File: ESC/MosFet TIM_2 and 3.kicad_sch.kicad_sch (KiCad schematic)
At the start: 34 parts, among them J3 Conn_01x03, Q1 BSC028N06LS3, Q2 BSC028N06LS3, U2 IRS2101

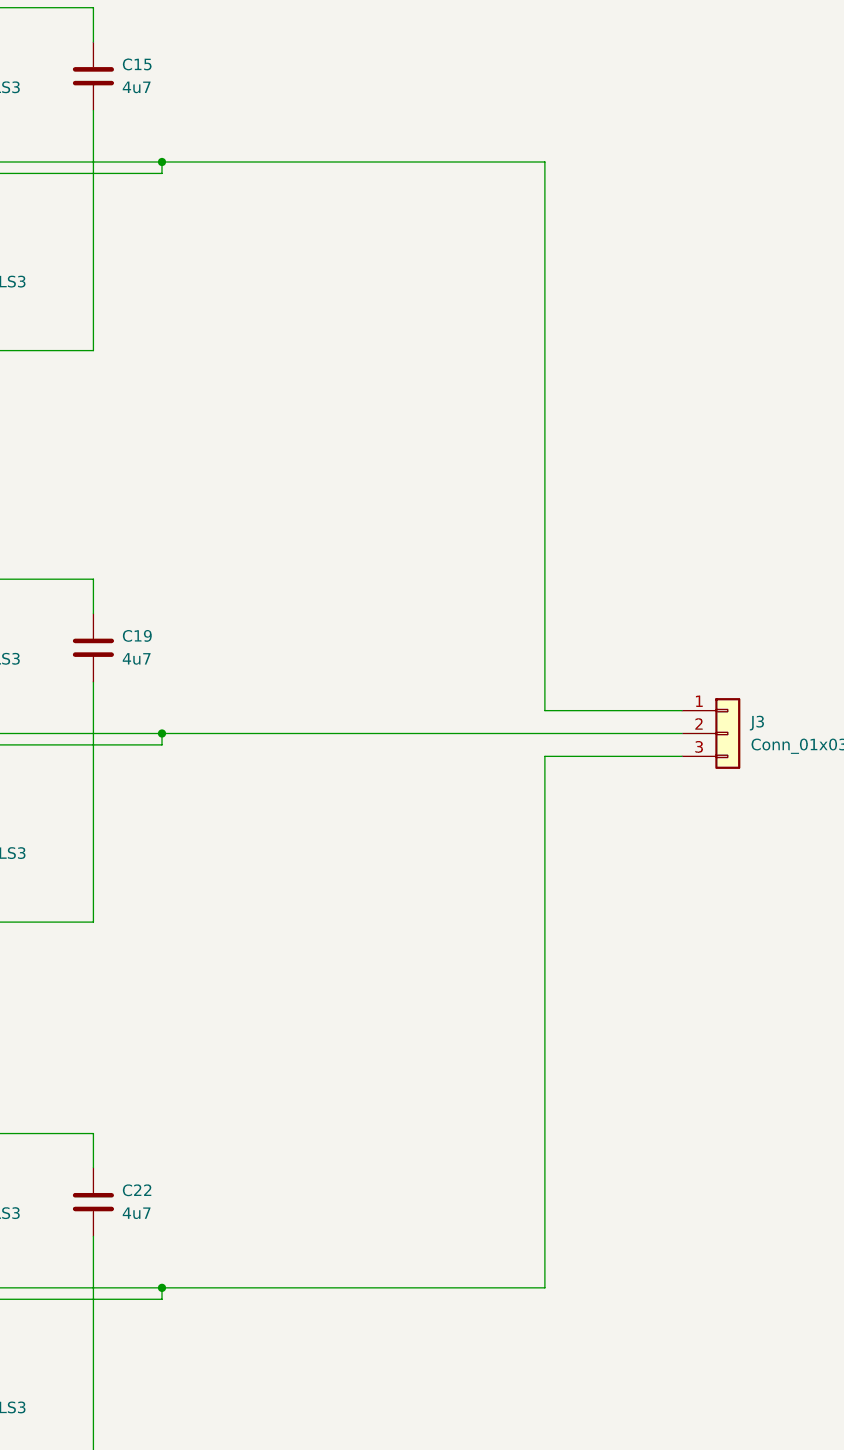
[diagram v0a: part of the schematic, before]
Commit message: finished a mockup of the pcb layout
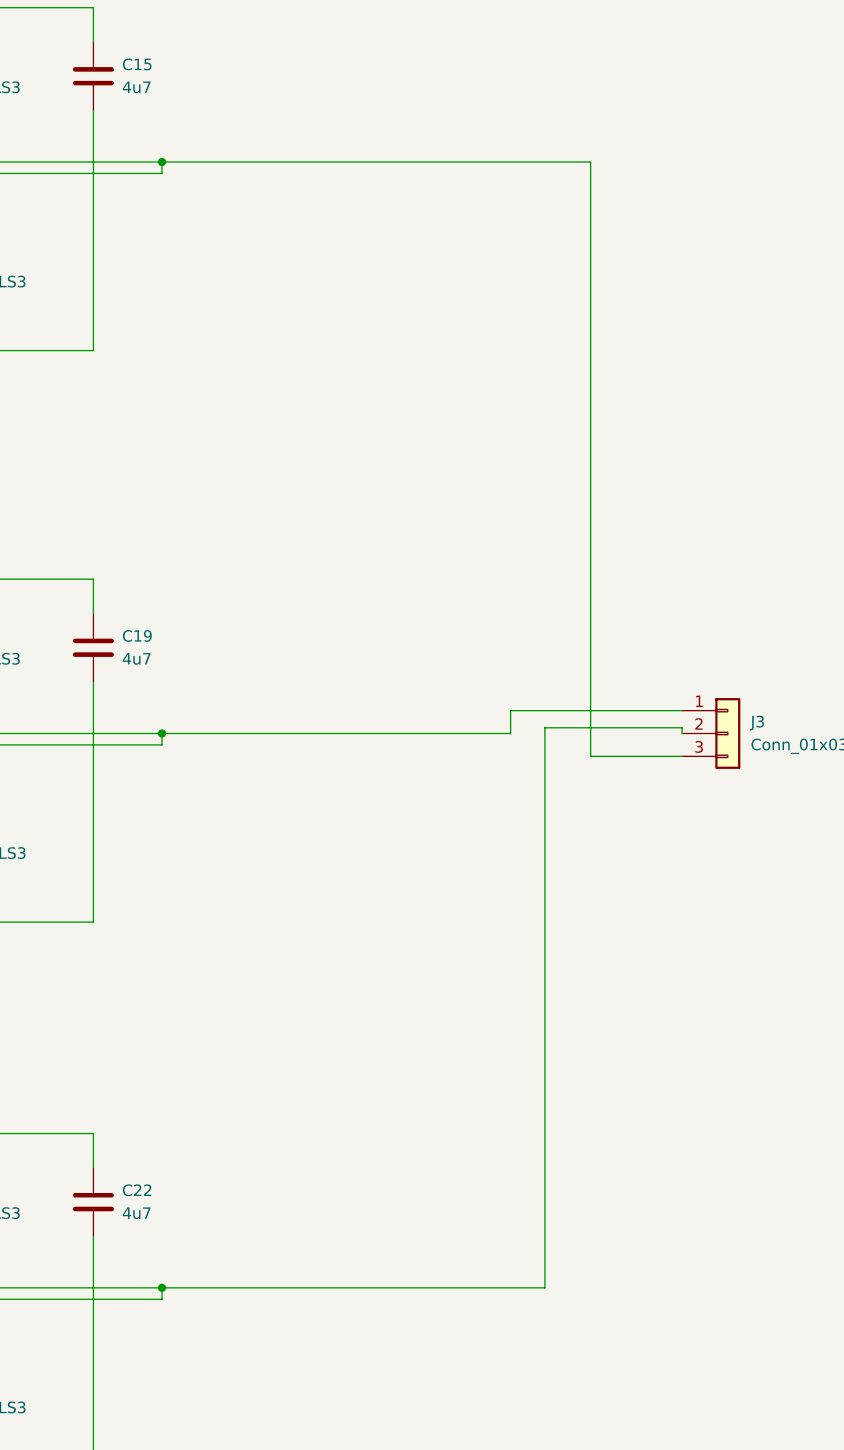
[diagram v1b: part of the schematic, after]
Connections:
- net at C14.2, Q1.5 (D), Q2.1 (S)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: now also J3.3 (Pin_3); no longer J3.1 (Pin_1)
- net at C20.2, Q1.5 (D), Q2.1 (S)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: now also J3.1 (Pin_1); no longer J3.2 (Pin_2)
- net at C23.2, Q1.5 (D), Q2.1 (S)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: now also J3.2 (Pin_2); no longer J3.3 (Pin_3)
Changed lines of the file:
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@@
   (junction (at 71.12 86.36) (diameter 0) (color 0 0 0 0)
   )
+  (junction (at 116.84 21.59) (diameter 0) (color 0 0 0 0)
+  )
+  (junction (at 54.61 38.735) (diameter 0) (color 0 0 0 0)
+  )
+  (junction (at 116.84 102.235) (diameter 0) (color 0 0 0 0)
+  )
+  (junction (at 81.915 31.115) (diameter 0) (color 0 0 0 0)
+  )
+  (junction (at 54.61 47.625) (diameter 0) (color 0 0 0 0)
+  )
+  (junction (at 116.84 184.785) (diameter 0) (color 0 0 0 0)
+  )
+  (junction (at 149.225 38.735) (diameter 0) (color 0 0 0 0)
+  )
+  (junction (at 81.915 43.815) (diameter 0) (color 0 0 0 0)
+  )
+  (junction (at 81.915 107.315) (diameter 0) (color 0 0 0 0)
+  )
+  (junction (at 81.915 168.91) (diameter 0) (color 0 0 0 0)
+  )
+  (junction (at 54.61 163.83) (diameter 0) (color 0 0 0 0)
+  )
+  (junction (at 54.61 171.45) (diameter 0) (color 0 0 0 0)
+  )
+  (junction (at 116.84 38.735) (diameter 0) (color 0 0 0 0)
+  )
+  (junction (at 54.61 109.855) (diameter 0) (color 0 0 0 0)
+  )
+  (junction (at 116.84 163.83) (diameter 0) (color 0 0 0 0)
+  )
+  (junction (at 116.84 85.09) (diameter 0) (color 0 0 0 0)
+  )
+  (junction (at 116.84 146.685) (diameter 0) (color 0 0 0 0)
+  )
+  (junction (at 116.84 59.69) (diameter 0) (color 0 0 0 0)
+  )
+  (junction (at 149.225 163.83) (diameter 0) (color 0 0 0 0)
+  )
+  (junction (at 116.84 123.19) (diameter 0) (color 0 0 0 0)
+  )
+  (junction (at 71.12 147.955) (diameter 0) (color 0 0 0 0)
+  )
+  (junction (at 71.12 22.86) (diameter 0) (color 0 0 0 0)
+  )
+  (junction (at 81.915 94.615) (diameter 0) (color 0 0 0 0)
+  )
+  (junction (at 81.915 156.21) (diameter 0) (color 0 0 0 0)
+  )
   (junction (at 149.225 102.235) (diameter 0) (color 0 0 0 0)
   )
-  (junction (at 116.84 21.59) (diameter 0) (color 0 0 0 0)
-  )
-  (junction (at 54.61 38.735) (diameter 0) (color 0 0 0 0)
-  )
-  (junction (at 116.84 102.235) (diameter 0) (color 0 0 0 0)
-  )
-  (junction (at 81.915 31.115) (diameter 0) (color 0 0 0 0)
-  )
-  (junction (at 54.61 47.625) (diameter 0) (color 0 0 0 0)
-  )
-  (junction (at 116.84 184.785) (diameter 0) (color 0 0 0 0)
-  )
-  (junction (at 81.915 43.815) (diameter 0) (color 0 0 0 0)
-  )
-  (junction (at 81.915 107.315) (diameter 0) (color 0 0 0 0)
-  )
-  (junction (at 81.915 168.91) (diameter 0) (color 0 0 0 0)
-  )
-  (junction (at 54.61 163.83) (diameter 0) (color 0 0 0 0)
-  )
-  (junction (at 54.61 171.45) (diameter 0) (color 0 0 0 0)
-  )
-  (junction (at 116.84 38.735) (diameter 0) (color 0 0 0 0)
-  )
-  (junction (at 149.225 38.735) (diameter 0) (color 0 0 0 0)
-  )
-  (junction (at 54.61 109.855) (diameter 0) (color 0 0 0 0)
-  )
-  (junction (at 116.84 163.83) (diameter 0) (color 0 0 0 0)
-  )
-  (junction (at 116.84 85.09) (diameter 0) (color 0 0 0 0)
-  )
-  (junction (at 116.84 146.685) (diameter 0) (color 0 0 0 0)
-  )
-  (junction (at 116.84 59.69) (diameter 0) (color 0 0 0 0)
-  )
-  (junction (at 149.225 163.83) (diameter 0) (color 0 0 0 0)
-  )
-  (junction (at 116.84 123.19) (diameter 0) (color 0 0 0 0)
-  )
-  (junction (at 71.12 147.955) (diameter 0) (color 0 0 0 0)
-  )
-  (junction (at 71.12 22.86) (diameter 0) (color 0 0 0 0)
-  )
-  (junction (at 81.915 94.615) (diameter 0) (color 0 0 0 0)
-  )
-  (junction (at 81.915 156.21) (diameter 0) (color 0 0 0 0)
-  )
   (wire (pts (xy 50.8 38.735) (xy 54.61 38.735))
     (stroke (width 0) (type default))
@@
     (stroke (width 0) (type default))
   )
+  (wire (pts (xy 149.225 38.735) (xy 196.85 38.735))
+    (stroke (width 0) (type default))
+  )
   (wire (pts (xy 71.12 82.55) (xy 71.12 86.36))
     (stroke (width 0) (type default))
@@
     (stroke (width 0) (type default))
   )
+  (wire (pts (xy 207.01 101.6) (xy 207.01 102.235))
+    (stroke (width 0) (type default))
+  )
   (wire (pts (xy 116.84 163.83) (xy 116.84 159.385))
     (stroke (width 0) (type default))
@@
     (stroke (width 0) (type default))
   )
+  (wire (pts (xy 149.225 102.235) (xy 187.96 102.235))
+    (stroke (width 0) (type default))
+  )
   (wire (pts (xy 106.045 175.895) (xy 109.22 175.895))
     (stroke (width 0) (type default))
@@
     (stroke (width 0) (type default))
   )
+  (wire (pts (xy 187.96 99.695) (xy 207.01 99.695))
+    (stroke (width 0) (type default))
+  )
   (wire (pts (xy 60.96 147.955) (xy 66.04 147.955))
     (stroke (width 0) (type default))
@@
     (stroke (width 0) (type default))
   )
-  (wire (pts (xy 149.225 102.235) (xy 207.01 102.235))
-    (stroke (width 0) (type default))
-  )
   (wire (pts (xy 78.74 43.815) (xy 81.915 43.815))
     (stroke (width 0) (type default))
@@
     (stroke (width 0) (type default))
   )
-  (wire (pts (xy 149.225 38.735) (xy 191.77 38.735))
-    (stroke (width 0) (type default))
-  )
   (wire (pts (xy 54.61 109.855) (xy 63.5 109.855))
     (stroke (width 0) (type default))
@@
     (stroke (width 0) (type default))
   )
+  (wire (pts (xy 196.85 104.775) (xy 207.01 104.775))
+    (stroke (width 0) (type default))
+  )
   (wire (pts (xy 106.045 171.45) (xy 106.045 175.895))
     (stroke (width 0) (type default))
@@
     (stroke (width 0) (type default))
   )
+  (wire (pts (xy 196.85 38.735) (xy 196.85 104.775))
+    (stroke (width 0) (type default))
+  )
   (wire (pts (xy 116.84 85.09) (xy 116.84 87.63))
     (stroke (width 0) (type default))
@@
     (stroke (width 0) (type default))
   )
+  (wire (pts (xy 187.96 102.235) (xy 187.96 99.695))
+    (stroke (width 0) (type default))
+  )
   (wire (pts (xy 106.045 154.305) (xy 109.22 154.305))
     (stroke (width 0) (type default))
@@
     (stroke (width 0) (type default))
   )
-  (wire (pts (xy 191.77 99.695) (xy 207.01 99.695))
-    (stroke (width 0) (type default))
-  )
   (wire (pts (xy 60.96 86.36) (xy 66.04 86.36))
     (stroke (width 0) (type default))
@@
     (stroke (width 0) (type default))
   )
-  (wire (pts (xy 191.77 38.735) (xy 191.77 99.695))
-    (stroke (width 0) (type default))
-  )
   (wire (pts (xy 78.74 107.315) (xy 81.915 107.315))
     (stroke (width 0) (type default))
@@
     (stroke (width 0) (type default))
   )
-  (wire (pts (xy 191.77 104.775) (xy 207.01 104.775))
-    (stroke (width 0) (type default))
-  )
   (wire (pts (xy 97.79 171.45) (xy 106.045 171.45))
     (stroke (width 0) (type default))
@@
     (stroke (width 0) (type default))
   )
+  (wire (pts (xy 191.77 101.6) (xy 207.01 101.6))
+    (stroke (width 0) (type default))
+  )
   (wire (pts (xy 97.79 97.155) (xy 106.045 97.155))
     (stroke (width 0) (type default))
@@
     (stroke (width 0) (type default))
   )
-  (wire (pts (xy 191.77 163.83) (xy 191.77 104.775))
+  (wire (pts (xy 191.77 101.6) (xy 191.77 163.83))
     (stroke (width 0) (type default))
   )
@@
   )
   (symbol (lib_id "Jumper:SolderJumper_2_Open") (at 54.61 106.045 90) (unit 1)
-    (in_bom yes) (on_board yes) (dnp no) (fields_autoplaced)
+    (in_bom yes) (on_board yes) (dnp no)
     (property "Reference" "JP2" (at 56.515 104.775 90)
       (effects (font (size 1.27 1.27)) (justify right))

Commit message: did some of the routing ofthe PCB
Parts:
- J3: footprint TerminalBlock_Phoenix:TerminalBlock_Phoenix_MKDS-1,5-3_1x03_P5.00mm_Horizontal -> Connector_AMASS:AMASS_MR30PW-FB_1x03_P3.50mm_Horizontal
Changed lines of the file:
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@@
       (effects (font (size 1.27 1.27)) (justify left))
     )
-    (property "Footprint" "TerminalBlock_Phoenix:TerminalBlock_Phoenix_MKDS-1,5-3_1x03_P5.00mm_Horizontal" (at 212.09 102.235 0)
+    (property "Footprint" "Connector_AMASS:AMASS_MR30PW-FB_1x03_P3.50mm_Horizontal" (at 212.09 102.235 0)
       (effects (font (size 1.27 1.27)) hide)
     )

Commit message: finished the pcb layout of the ESC and now need to be revised to make sure everything is correct
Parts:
- removed C13, C18, C21: 100n 50V, Capacitor_SMD:C_0603_1608Metric_Pad1.08x0.95mm_HandSolder, symbol Device:C_Small
- removed C14, C20, C23: 2u7 50V, Capacitor_SMD:C_0603_1608Metric_Pad1.08x0.95mm_HandSolder, symbol Device:C
- removed C15, C19, C22: 4u7, Capacitor_SMD:C_0603_1608Metric_Pad1.08x0.95mm_HandSolder, symbol Device:C
- removed D1, D2, D3: D, Diode_SMD:D_0603_1608Metric_Pad1.05x0.95mm_HandSolder, symbol Device:D
- removed J3: Conn_01x03, Connector_AMASS:AMASS_MR30PW-FB_1x03_P3.50mm_Horizontal, symbol Connector_Generic:Conn_01x03
- removed JP1, JP2, JP3, JP4, JP5, JP6: jump, Capacitor_SMD:C_0603_1608Metric_Pad1.08x0.95mm_HandSolder, symbol Jumper:SolderJumper_2_Open
- removed Q1 (x3), Q2 (x3): BSC028N06LS3, Package_TO_SOT_SMD:TDSON-8-1, symbol Transistor_FET:BSC028N06LS3
- removed R1, R2, R5, R6, R7, R8: 200, Resistor_SMD:R_2512_6332Metric_Pad1.40x3.35mm_HandSolder, symbol Device:R
- removed U2 (x3): IRS2101, Package_SO:SOIC-8-1EP_3.9x4.9mm_P1.27mm_EP2.41x3.81mm, symbol Driver_FET:IRS2101
